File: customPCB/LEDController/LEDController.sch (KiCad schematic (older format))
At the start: 23 parts

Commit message: added board design
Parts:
- removed SW?: SW_Push_Dual, symbol Switch:SW_Push_Dual
- added D1: MBR120, Diode_SMD:D_SOD-123F, symbol Device:D_Schottky_Small
- added H1, H2, H3, H4: MountingHole_Pad, MountingHole:MountingHole_3.2mm_M3_Pad_Via, symbol Mechanical:MountingHole_Pad
- added J2: Barrel_Jack_MountingPin, Connector_BarrelJack:BarrelJack_CUI_PJ-063AH_Horizontal, symbol Connector:Barrel_Jack_MountingPin
- added J3, J4: Conn_01x03, Connector_PinHeader_2.54mm:PinHeader_1x03_P2.54mm_Vertical, symbol Connector_Generic:Conn_01x03
- added J5, J6: Conn_01x02, Connector_PinHeader_2.54mm:PinHeader_1x02_P2.54mm_Vertical, symbol Connector_Generic:Conn_01x02
- added R5: 10K, Resistor_SMD:R_0603_1608Metric, symbol Device:R_Small_US
- added SW1: KMR2, Button_Switch_SMD:SW_Push_1P1T_NO_CK_KMR2, symbol Switch:SW_Push
- C1, C2, C3, C4, C5, C6: renamed from C?; footprint (none) -> Capacitor_SMD:C_0603_1608Metric
- D2, D3: renamed from D?; footprint (none) -> LED_SMD:LED_0603_1608Metric
- J1: renamed from J?; footprint (none) -> Connector_USB:USB_Micro-B_Amphenol_10103594-0001LF_Horizontal
- Q2, Q3: renamed from Q?; footprint SOT23-3 -> Silicon-Standard:SOT23-3
- R1, R2, R3, R4, R6, R7, R8: renamed from R?; footprint (none) -> Resistor_SMD:R_0603_1608Metric
- gave numbers to parts that had none: 4
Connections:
- net +3V3: now also J4.1 (Pin_1), J5.1 (Pin_1), R5.2
- net GND: now also H1.1, H2.1, H3.1, H4.1, J2.2, J2.MP (MountPin), J3.3 (Pin_3), J4.3 (Pin_3), J6.2 (Pin_2), R5.1, SW1.2
- net LED_PIN: now also U2.9 (IO33), J3.2 (Pin_2); no longer U2.8 (IO32)
- net RESET: now also SW1.1
- net VCC: now also D1.2 (A), J2.1; no longer C1.1, Q1.2 (S), R1.1, R2.1, U1.1 (VIN)
- net BUTTON: now reaches U2.10 (IO25)
- net BUTTON: now also J5.2 (Pin_2)
- net GPIO: now reaches U2.11 (IO26)
- net GPIO: now also J6.1 (Pin_1)
- new net +5V: C1.1, D1.1 (K), J3.1 (Pin_1), Q1.2 (S), R1.1, R2.1, U1.1 (VIN)
- new net DIAL_PIN: J4.2 (Pin_2), U2.8 (IO32)
- no-connect marks 0 -> 38
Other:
- note added: "Connectors"
- note added: "Mounting Holes"
- moved on the sheet: C2, Q1

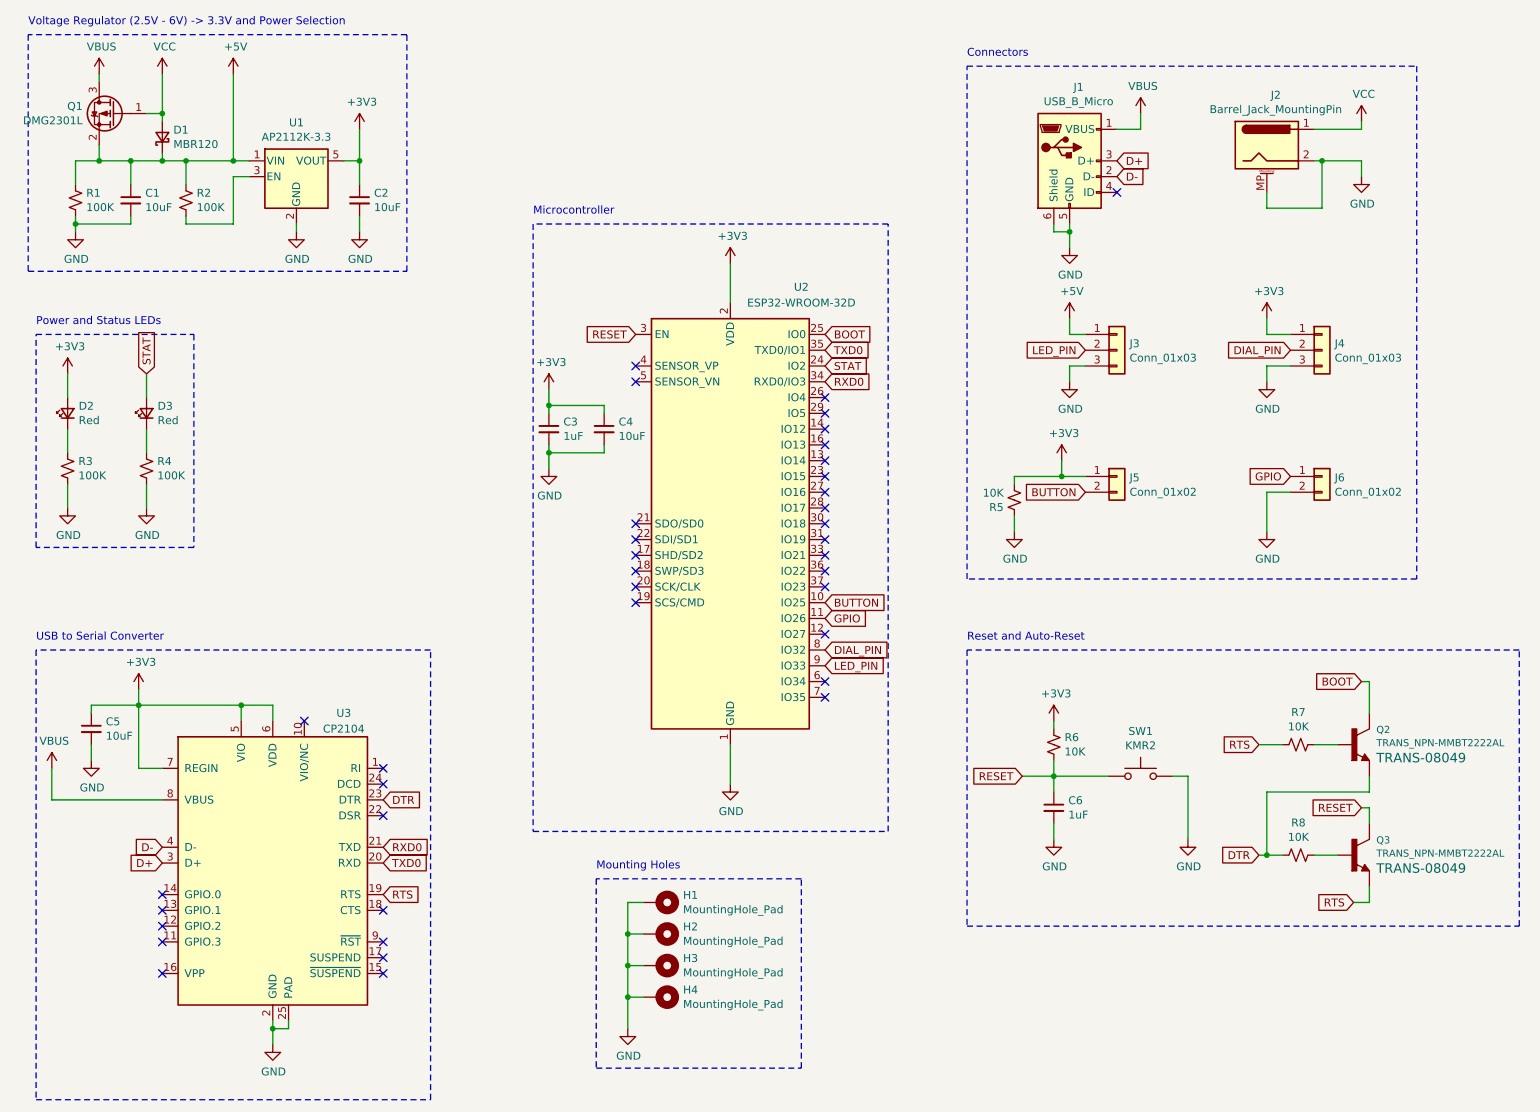
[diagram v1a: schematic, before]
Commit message: added off button
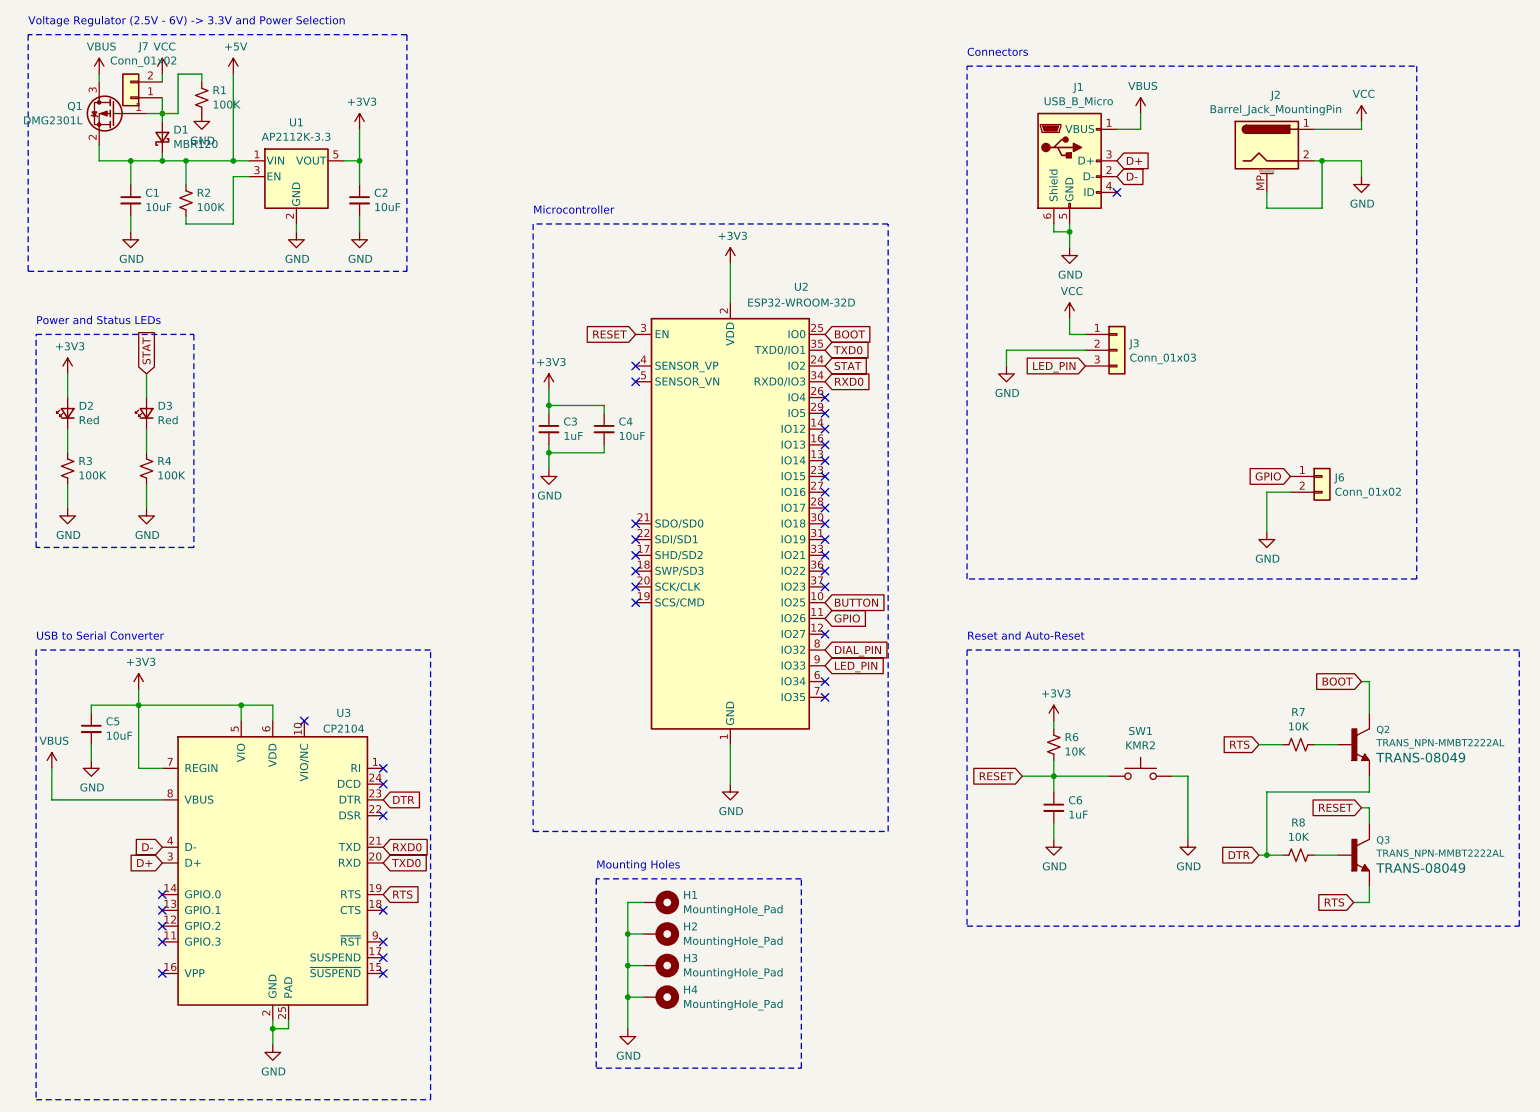
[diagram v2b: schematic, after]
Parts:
- removed J4: Conn_01x03, Connector_PinHeader_2.54mm:PinHeader_1x03_P2.54mm_Vertical, symbol Connector_Generic:Conn_01x03
- removed J5: Conn_01x02, Connector_PinHeader_2.54mm:PinHeader_1x02_P2.54mm_Vertical, symbol Connector_Generic:Conn_01x02
- removed R5: 10K, Resistor_SMD:R_0603_1608Metric, symbol Device:R_Small_US
- added J7: Conn_01x02, Connector_PinHeader_2.54mm:PinHeader_1x02_P2.54mm_Vertical, symbol Connector_Generic:Conn_01x02
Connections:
- net +5V: no longer J3.1 (Pin_1), R1.1
- net GND: now also J3.2 (Pin_2); no longer J3.3 (Pin_3)
- net LED_PIN: now also J3.3 (Pin_3); no longer J3.2 (Pin_2)
- net VCC: now also J3.1 (Pin_1), J7.2 (Pin_2); no longer D1.2 (A), Q1.1 (G)
- new net: D1.2 (A), J7.1 (Pin_1), Q1.1 (G), R1.1
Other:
- moved on the sheet: R1
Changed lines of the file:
@@
 L Device:R_Small_US R1
 U 1 1 5EEC1C2F
-P 1300 1700
-F 0 "R1" H 1368 1746 50  0000 L CNN
-F 1 "100K" H 1368 1655 50  0000 L CNN
-F 2 "Resistor_SMD:R_0603_1608Metric" H 1300 1700 50  0001 C CNN
-F 3 "~" H 1300 1700 50  0001 C CNN
-	1    1300 1700
-	1    0    0    -1
-$EndComp
-Wire Wire Line
-	1300 1600 1300 1450
+P 2100 1050
+F 0 "R1" H 2168 1096 50  0000 L CNN
+F 1 "100K" H 2168 1005 50  0000 L CNN
+F 2 "Resistor_SMD:R_0603_1608Metric" H 2100 1050 50  0001 C CNN
+F 3 "~" H 2100 1050 50  0001 C CNN
+	1    2100 1050
+	1    0    0    -1
+$EndComp
 $Comp
 L power:GND #PWR08
 U 1 1 5EEC2F97
-P 1300 1900
-F 0 "#PWR08" H 1300 1650 50  0001 C CNN
-F 1 "GND" H 1305 1727 50  0000 C CNN
-F 2 "" H 1300 1900 50  0001 C CNN
-F 3 "" H 1300 1900 50  0001 C CNN
-	1    1300 1900
+P 1650 1900
+F 0 "#PWR08" H 1650 1650 50  0001 C CNN
+F 1 "GND" H 1655 1727 50  0000 C CNN
+F 2 "" H 1650 1900 50  0001 C CNN
+F 3 "" H 1650 1900 50  0001 C CNN
+	1    1650 1900
 	1    0    0    -1
 $EndComp
@@
 $EndComp
 Wire Wire Line
-	1300 1800 1300 1850
-Wire Wire Line
 	1650 1600 1650 1450
-Wire Wire Line
-	1650 1800 1650 1850
-Wire Wire Line
-	1650 1850 1300 1850
-Connection ~ 1300 1850
-Wire Wire Line
-	1300 1850 1300 1900
 Wire Wire Line
 	2000 1600 2000 1450
@@
 	1850 1150 1850 1200
 Wire Wire Line
-	1850 900  1850 1150
+	1850 900  1850 950
 Connection ~ 1850 1150
 Wire Notes Line
@@
 L power:GND #PWR016
 U 1 1 5EEEA90C
-P 7600 2850
-F 0 "#PWR016" H 7600 2600 50  0001 C CNN
-F 1 "GND" H 7605 2677 50  0000 C CNN
-F 2 "" H 7600 2850 50  0001 C CNN
-F 3 "" H 7600 2850 50  0001 C CNN
-	1    7600 2850
+P 7200 2750
+F 0 "#PWR016" H 7200 2500 50  0001 C CNN
+F 1 "GND" H 7205 2577 50  0000 C CNN
+F 2 "" H 7200 2750 50  0001 C CNN
+F 3 "" H 7200 2750 50  0001 C CNN
+	1    7200 2750
 	1    0    0    -1
 $EndComp
@@
 Wire Wire Line
 	7600 2550 7600 2450
-Wire Wire Line
-	7700 2750 7600 2750
-Wire Wire Line
-	7600 2750 7600 2850
-Text GLabel 7700 2650 0    50   Input ~ 0
+Text GLabel 7700 2750 0    50   Input ~ 0
 LED_PIN
 Text GLabel 6050 4550 2    50   Input ~ 0
 DIAL_PIN
-$Comp
-L Connector_Generic:Conn_01x03 J4
-U 1 1 5EEF39A4
-P 9200 2650
-F 0 "J4" H 9280 2692 50  0000 L CNN
-F 1 "Conn_01x03" H 9280 2601 50  0000 L CNN
-F 2 "Connector_PinHeader_2.54mm:PinHeader_1x03_P2.54mm_Vertical" H 9200 2650 50  0001 C CNN
-F 3 "~" H 9200 2650 50  0001 C CNN
-	1    9200 2650
-	1    0    0    -1
-$EndComp
-Text GLabel 9000 2650 0    50   Input ~ 0
-DIAL_PIN
-$Comp
-L power:+3V3 #PWR014
-U 1 1 5EEF46C3
-P 8850 2450
-F 0 "#PWR014" H 8850 2300 50  0001 C CNN
-F 1 "+3V3" H 8865 2623 50  0000 C CNN
-F 2 "" H 8850 2450 50  0001 C CNN
-F 3 "" H 8850 2450 50  0001 C CNN
-	1    8850 2450
-	1    0    0    -1
-$EndComp
-$Comp
-L power:GND #PWR017
-U 1 1 5EEF4EE0
-P 8850 2850
-F 0 "#PWR017" H 8850 2600 50  0001 C CNN
-F 1 "GND" H 8855 2677 50  0000 C CNN
-F 2 "" H 8850 2850 50  0001 C CNN
-F 3 "" H 8850 2850 50  0001 C CNN
-	1    8850 2850
-	1    0    0    -1
-$EndComp
-Wire Wire Line
-	9000 2750 8850 2750
-Wire Wire Line
-	8850 2750 8850 2850
-Wire Wire Line
-	9000 2550 8850 2550
-Wire Wire Line
-	8850 2550 8850 2450
-$Comp
-L Connector_Generic:Conn_01x02 J5
-U 1 1 5EF030E8
-P 7900 3450
-F 0 "J5" H 7980 3442 50  0000 L CNN
-F 1 "Conn_01x02" H 7980 3351 50  0000 L CNN
-F 2 "Connector_PinHeader_2.54mm:PinHeader_1x02_P2.54mm_Vertical" H 7900 3450 50  0001 C CNN
-F 3 "~" H 7900 3450 50  0001 C CNN
-	1    7900 3450
-	1    0    0    -1
-$EndComp
 Text GLabel 6050 4250 2    50   Input ~ 0
 BUTTON
@@
 	1    0    0    -1
 $EndComp
-$Comp
-L power:+3V3 #PWR019
-U 1 1 5EF0755E
-P 7550 3350
-F 0 "#PWR019" H 7550 3200 50  0001 C CNN
-F 1 "+3V3" H 7565 3523 50  0000 C CNN
-F 2 "" H 7550 3350 50  0001 C CNN
-F 3 "" H 7550 3350 50  0001 C CNN
-	1    7550 3350
-	1    0    0    -1
-$EndComp
-Wire Wire Line
-	7550 3350 7550 3450
-Wire Wire Line
-	7550 3450 7700 3450
-$Comp
-L Device:R_Small_US R5
-U 1 1 5EF0BF19
-P 7250 3600
-F 0 "R5" H 7318 3646 50  0000 L CNN
-F 1 "10K" H 7318 3555 50  0000 L CNN
-F 2 "Resistor_SMD:R_0603_1608Metric" H 7250 3600 50  0001 C CNN
-F 3 "~" H 7250 3600 50  0001 C CNN
-	1    7250 3600
-	-1   0    0    1
-$EndComp
-Connection ~ 7550 3450
-$Comp
-L power:GND #PWR023
-U 1 1 5EF10C6C
-P 7250 3800
-F 0 "#PWR023" H 7250 3550 50  0001 C CNN
-F 1 "GND" H 7255 3627 50  0000 C CNN
-F 2 "" H 7250 3800 50  0001 C CNN
-F 3 "" H 7250 3800 50  0001 C CNN
-	1    7250 3800
-	1    0    0    -1
-$EndComp
-Text GLabel 7700 3550 0    50   Input ~ 0
-BUTTON
-Wire Wire Line
-	7250 3450 7250 3500
-Wire Wire Line
-	7250 3450 7550 3450
-Wire Wire Line
-	7250 3700 7250 3800
 $Comp
 L power:GND #PWR024
@@
 NoConn ~ 1850 6100
 Wire Wire Line
-	1300 1450 1450 1450
-Wire Wire Line
 	1450 1450 1650 1450
-Connection ~ 1450 1450
 Wire Wire Line
 	1650 1450 1850 1450
@@
 Wire Wire Line
 	2300 1450 2400 1450
-$Comp
-L power:+5V #PWR013
-U 1 1 5EFE2048
-P 7600 2450
-F 0 "#PWR013" H 7600 2300 50  0001 C CNN
-F 1 "+5V" H 7615 2623 50  0000 C CNN
-F 2 "" H 7600 2450 50  0001 C CNN
-F 3 "" H 7600 2450 50  0001 C CNN
-	1    7600 2450
-	1    0    0    -1
-$EndComp
 $Comp
 L Switch:SW_Push SW1
@@
 Wire Wire Line
 	9200 1450 9450 1450
+Wire Wire Line
+	1650 1800 1650 1900
+Wire Wire Line
+	2100 950  2100 900
+$Comp
+L power:GND #PWR0101
+U 1 1 5F0F4D54
+P 2100 1150
+F 0 "#PWR0101" H 2100 900 50  0001 C CNN
+F 1 "GND" H 2105 977 50  0000 C CNN
+F 2 "" H 2100 1150 50  0001 C CNN
+F 3 "" H 2100 1150 50  0001 C CNN
+	1    2100 1150
+	1    0    0    -1
+$EndComp
+$Comp
+L power:VCC #PWR0102
+U 1 1 5F13AE88
+P 7600 2450
+F 0 "#PWR0102" H 7600 2300 50  0001 C CNN
+F 1 "VCC" H 7615 2623 50  0000 C CNN
+F 2 "" H 7600 2450 50  0001 C CNN
+F 3 "" H 7600 2450 50  0001 C CNN
+	1    7600 2450
+	1    0    0    -1
+$EndComp
+Wire Wire Line
+	7200 2650 7200 2750
+Wire Wire Line
+	7200 2650 7700 2650
+$Comp
+L Connector_Generic:Conn_01x02 J7
+U 1 1 5EF2B1B7
+P 1650 1050
+F 0 "J7" H 1568 725 50  0000 C CNN
+F 1 "Conn_01x02" H 1568 816 50  0000 C CNN
+F 2 "Connector_PinHeader_2.54mm:PinHeader_1x02_P2.54mm_Vertical" H 1650 1050 50  0001 C CNN
+F 3 "~" H 1650 1050 50  0001 C CNN
+	1    1650 1050
+	-1   0    0    1
+$EndComp
+Wire Wire Line
+	1850 1050 1850 1150
+Wire Wire Line
+	2100 900  1950 900
+Wire Wire Line
+	1950 900  1950 1150
+Wire Wire Line
+	1950 1150 1850 1150
 $EndSCHEMATC
